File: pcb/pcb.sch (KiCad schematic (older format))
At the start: 20 parts, among them J1 BAT+, J2 BAT-, J3 Molex, SW1 Reset, SW2 Flash, U1 CP2102-BREAKOUT, U2 ESP-12F, U3 TP4056, U4 GY-521, U5 VREG

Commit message: Patent-unencumbered PCB concept
Tilting is off the table, so let's explore a different idea: weighing
a sinker immersed in the wort. See the github pages plog for more.
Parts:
- removed U4: GY-521, GY521:GY521, symbol GY-521
- added D1, D2: D, Diodes_SMD:D_0805, symbol D
- added J10: GRN, Extra_Pads:SolderWirePad_single_SMD_5x3mm, symbol Conn_01x01
- added J11: RED, Extra_Pads:SolderWirePad_single_SMD_5x3mm, symbol Conn_01x01
- added J12: Load Cell, Connectors_Molex:Molex_PicoBlade_53048-0410_04x1.25mm_Angled, symbol Conn_01x04
- added J4: TMP37, Connectors_Molex:Molex_PicoBlade_53048-0310_03x1.25mm_Angled, symbol Conn_01x03
- added J5: TMP+, Extra_Pads:SolderWirePad_single_SMD_5x3mm, symbol Conn_01x01
- added J6: TMPO, Extra_Pads:SolderWirePad_single_SMD_5x3mm, symbol Conn_01x01
- added J7: TMP-, Extra_Pads:SolderWirePad_single_SMD_5x3mm, symbol Conn_01x01
- added J8: WHT, Extra_Pads:SolderWirePad_single_SMD_5x3mm, symbol Conn_01x01
- added J9: BLK, Extra_Pads:SolderWirePad_single_SMD_5x3mm, symbol Conn_01x01
- added Q1: BC847, TO_SOT_Packages_SMD:SOT-23, symbol BC847
- added R8: 10k, Resistors_SMD:R_0805, symbol R
- added U4: HX711_BREAKOUT, HX711-XNQ:HX711-XNQ, symbol HX711_BREAKOUT
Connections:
- net labels added: ADC, BLK, CLK, DAT, GRN, HX+, RED, SENS1, SENS2, TMP+, TMP-, TMPO, WHT
- net labels removed: GY+, SCL, SDA
- wire segments 61 -> 86
- no-connect marks 14 -> 10
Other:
- note added: "Battery Monitor"
- note added: "Battery Pads\n\n"
- note added: "Load Cell"
- note added: "TMP37 Molex/Pads"
- note removed: "Pad"
- moved on the sheet: C1, R1, R2, R3, R4, R5, R6, R7, SW1, SW2, U2

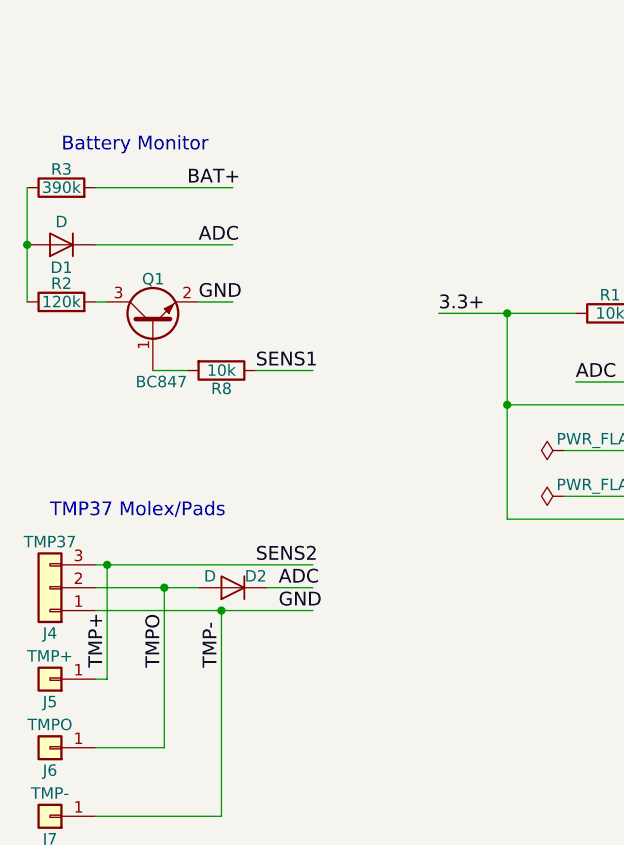
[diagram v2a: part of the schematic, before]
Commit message: Add a pad for a decoupling capacitor for temperature sensor, just in case
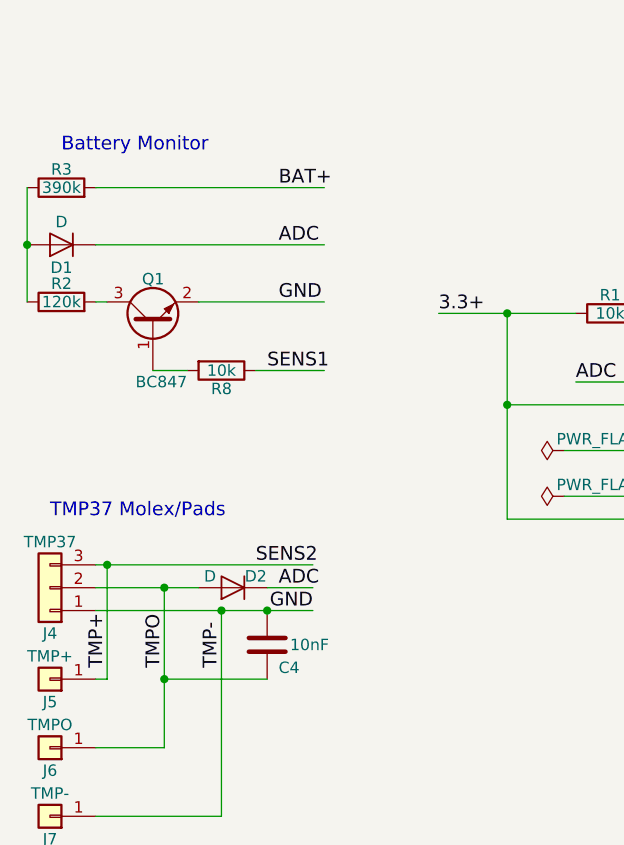
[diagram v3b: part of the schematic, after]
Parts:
- added C4: 10nF, Capacitors_SMD:C_0805, symbol C
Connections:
- wire segments 86 -> 87
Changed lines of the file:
@@
 Text Label 3800 2500 0    60   ~ 0
 USB-
-Text Label 1550 4250 0    60   ~ 0
+Text Label 1950 4250 0    60   ~ 0
 BAT+
 Text Label 6000 5200 0    60   ~ 0
@@
 	0    -1   -1   0
 $EndComp
-Text Label 1600 4750 0    60   ~ 0
+Text Label 1950 4750 0    60   ~ 0
 GND
 $Comp
@@
 	-1   0    0    1
 $EndComp
-Text Label 1600 4500 0    60   ~ 0
+Text Label 1950 4500 0    60   ~ 0
 ADC
 Text Label 3600 5500 0    60   ~ 0
@@
 	0    -1   -1   0
 $EndComp
-Text Label 1850 5050 0    60   ~ 0
+Text Label 1900 5050 0    60   ~ 0
 SENS1
 Text Notes 1000 4100 0    60   ~ 0
@@
 Text Label 1850 5900 0    60   ~ 0
 SENS2
-Text Label 1950 6100 0    60   ~ 0
+Text Label 2100 6100 2    60   ~ 0
 GND
 $Comp
@@
 	3950 5100 3250 5100
 Wire Wire Line
-	1150 4500 1750 4500
+	1150 4500 2150 4500
 Wire Wire Line
 	3600 5500 3950 5500
@@
 	3200 5600 3950 5600
 Wire Wire Line
-	1150 4250 1750 4250
+	1150 4250 2150 4250
 Wire Wire Line
 	850  4250 850  4750
@@
 	1150 4750 1200 4750
 Wire Wire Line
-	1600 4750 1750 4750
+	1600 4750 2150 4750
 Wire Wire Line
 	1150 5900 2100 5900
@@
 	1400 5050 1550 5050
 Wire Wire Line
-	1850 5050 2100 5050
+	1850 5050 2150 5050
+$Comp
+L C C4
+U 1 1 5B2A9325
+P 1900 6250
+F 0 "C4" H 1950 6150 50  0000 L CNN
+F 1 "10nF" H 2000 6250 50  0000 L CNN
+F 2 "Capacitors_SMD:C_0805" H 1938 6100 50  0001 C CNN
+F 3 "" H 1900 6250 50  0001 C CNN
+	1    1900 6250
+	1    0    0    -1
+$EndComp
+Connection ~ 1900 6100
+Wire Wire Line
+	1450 6400 1900 6400
+Connection ~ 1450 6400
 $EndSCHEMATC

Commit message: Measure some pictures of chips to update local parts libraries
Hopefully it's good enough. Otherwise we'll fix it in rev2.
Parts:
- U4: footprint HX711-XNQ:HX711-XNQ -> HX711-XNQ:HX711-MINI
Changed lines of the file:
@@
 F 0 "U4" H 9150 5250 60  0000 C CNN
 F 1 "HX711_BREAKOUT" H 9150 5900 60  0000 C CNN
-F 2 "HX711-XNQ:HX711-XNQ" H 8650 5850 60  0001 C CNN
+F 2 "HX711-XNQ:HX711-MINI" H 8650 5850 60  0001 C CNN
 F 3 "" H 8650 5850 60  0001 C CNN
 	1    8650 5850

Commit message: Fix some design errors, including a missing connection from 16->RST
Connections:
- wire segments 87 -> 89
- no-connect marks 10 -> 9
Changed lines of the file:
@@
 	0    1    1    0
 $EndComp
-NoConn ~ 3950 5300
 $Comp
 L C C3
@@
 	6300 5600 6450 5600
 Wire Wire Line
-	3900 5000 3950 5000
+	3650 5000 3950 5000
 Wire Wire Line
 	5400 2250 5400 1950
@@
 	1450 6400 1900 6400
 Connection ~ 1450 6400
+Wire Wire Line
+	3950 5300 3650 5300
+Wire Wire Line
+	3650 5300 3650 5000
+Connection ~ 3900 5000
 $EndSCHEMATC

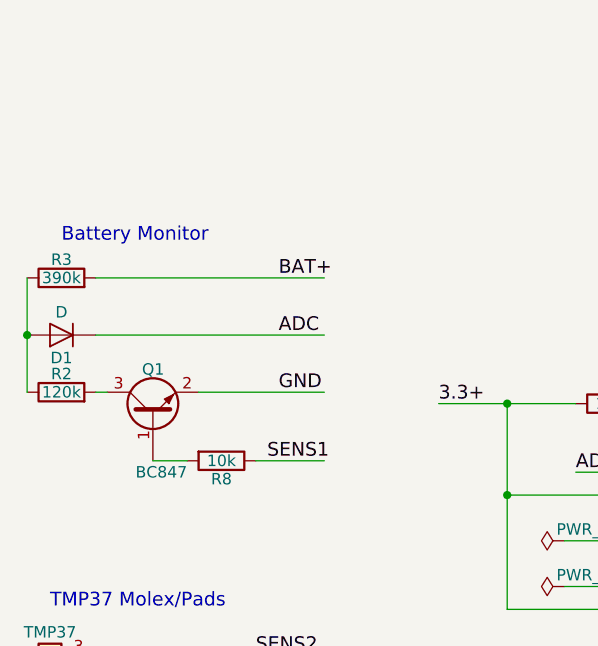
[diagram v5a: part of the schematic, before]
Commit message: Switch to p-channel MOSFET for battery monitor switch
Because we want as close to zero voltage through the circuit to the
ADC as possible when the battery monitor is off and the temperature
sensor is on, we need to switch on the high side, between BAT+ and
ADC.

The BSS84 seems like a reasonable choice; its maximum gate threshold
voltage is well below the difference between ground and a discharged
li-ion at 2.7V. I don't really care about pulling it up to 3.3 so
that it keeps the battery circuit off; it's the difference between
a hundred nanoamps and six or eight microamps.
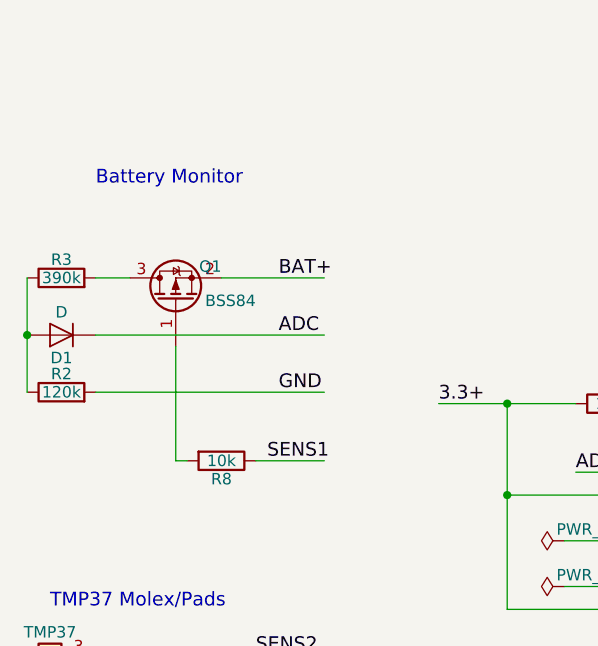
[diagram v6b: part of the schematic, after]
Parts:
- removed Q1: BC847, TO_SOT_Packages_SMD:SOT-23, symbol BC847
- added Q1: BSS84, TO_SOT_Packages_SMD:SOT-23, symbol BSS84
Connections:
- wire segments 89 -> 90
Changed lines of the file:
@@
 Text Label 3600 5400 0    60   ~ 0
 SENS2
-$Comp
-L BC847 Q1
-U 1 1 5B296BA7
-P 1400 4850
-F 0 "Q1" V 1600 4800 50  0000 L CNN
-F 1 "BC847" V 1150 4700 50  0000 L CNN
-F 2 "TO_SOT_Packages_SMD:SOT-23" H 1600 4775 50  0001 L CIN
-F 3 "" H 1400 4850 50  0001 L CNN
-	1    1400 4850
-	0    -1   -1   0
-$EndComp
 Text Label 1900 5050 0    60   ~ 0
 SENS1
-Text Notes 1000 4100 0    60   ~ 0
+Text Notes 1150 3850 0    60   ~ 0
 Battery Monitor
 $Comp
@@
 	3200 5600 3950 5600
 Wire Wire Line
-	1150 4250 2150 4250
-Wire Wire Line
 	850  4250 850  4750
 Connection ~ 850  4500
 Wire Wire Line
-	1150 4750 1200 4750
-Wire Wire Line
-	1600 4750 2150 4750
+	1150 4750 2150 4750
 Wire Wire Line
 	1150 5900 2100 5900
@@
 $EndComp
 Wire Wire Line
-	1400 5050 1550 5050
-Wire Wire Line
 	1850 5050 2150 5050
 $Comp
@@
 	3650 5300 3650 5000
 Connection ~ 3900 5000
+$Comp
+L BSS84 Q1
+U 1 1 5B2BFF6A
+P 1500 4350
+F 0 "Q1" V 1650 4150 50  0000 L CNN
+F 1 "BSS84" V 1500 4000 50  0000 L CNN
+F 2 "TO_SOT_Packages_SMD:SOT-23" H 1700 4275 50  0001 L CIN
+F 3 "" H 1500 4350 50  0001 L CNN
+	1    1500 4350
+	0    -1   -1   0
+$EndComp
+Wire Wire Line
+	1150 4250 1300 4250
+Wire Wire Line
+	1700 4250 2150 4250
+Wire Wire Line
+	1500 4550 1500 5050
+Wire Wire Line
+	1500 5050 1550 5050
 $EndSCHEMATC

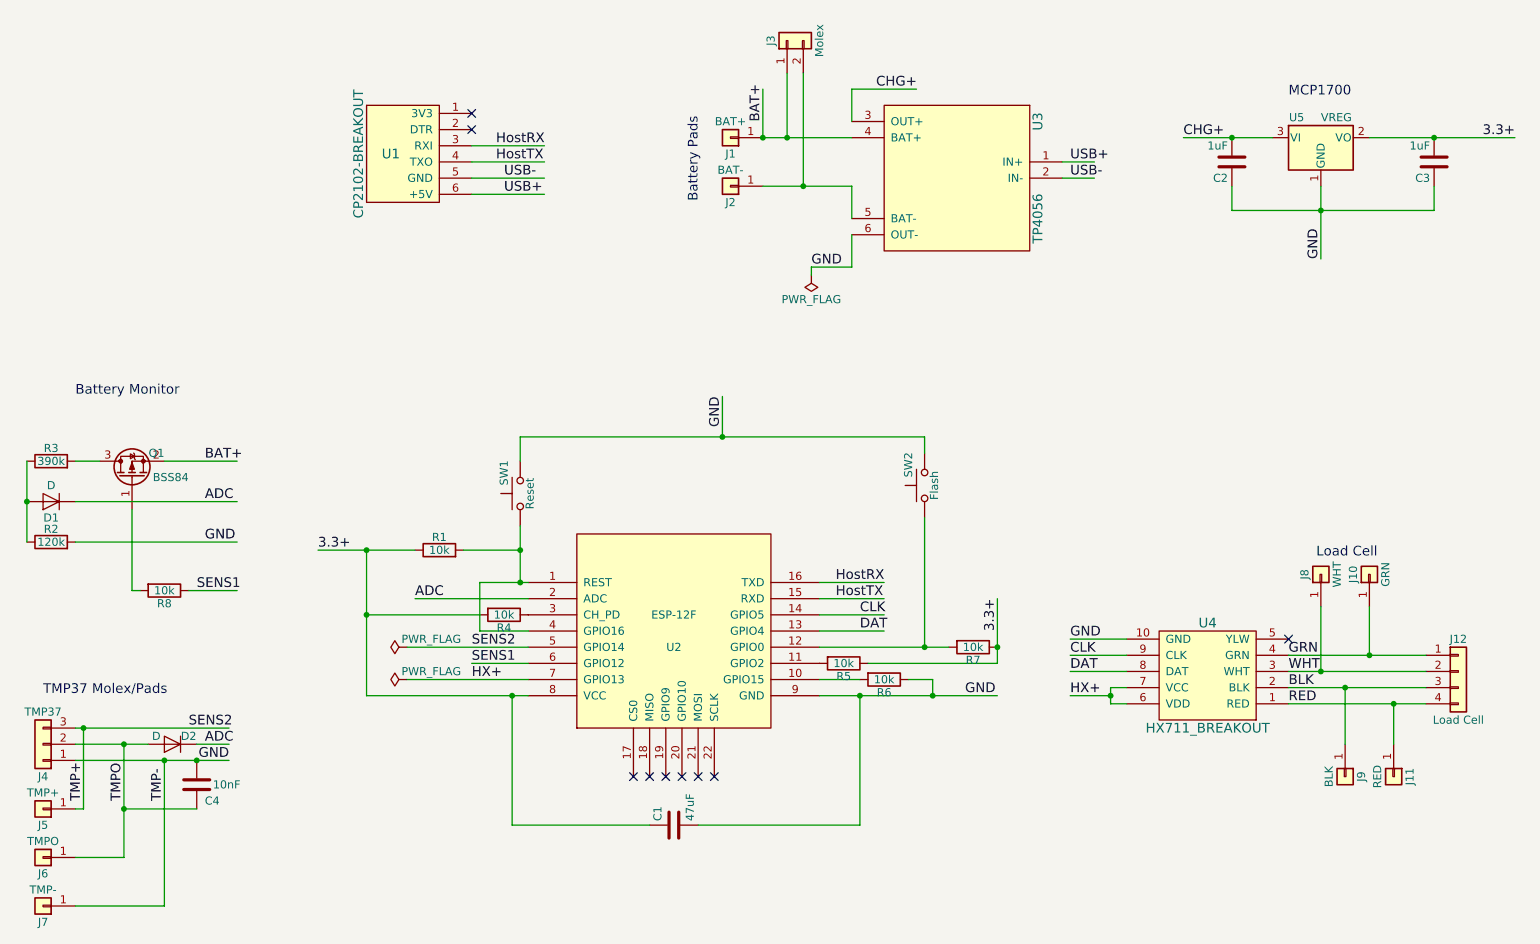
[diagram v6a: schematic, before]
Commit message: DS18B20, 4x3 switch footprint, routing tweaks
Use a DS18B20 temperature sensor instead of a TMP36. We have enough
GPIOs—we can drive it from the former SENS2 net (power for the prior
sensor) and use the former SENS1 net (battery monitor transistor) for
the data line. This simplifies the ADC circuitry significantly, and
lets us ditch a bunch of parts.

Add 4mmx3mm switch footprint, adjust routing as needed.
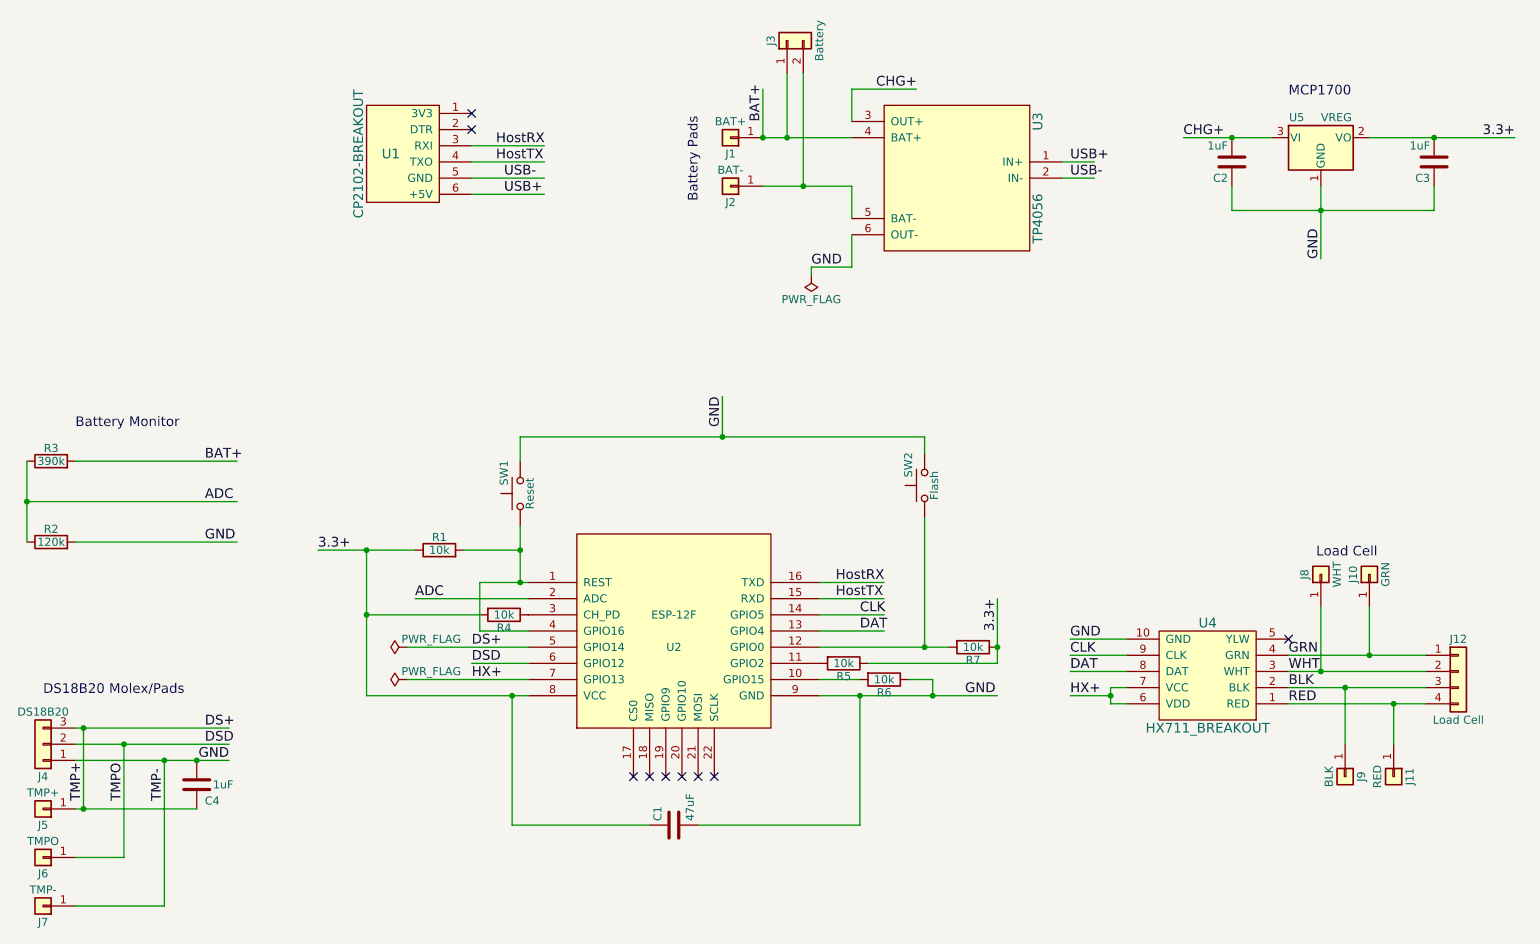
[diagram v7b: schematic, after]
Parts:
- removed D1, D2: D, Diodes_SMD:D_0805, symbol D
- removed Q1: BSS84, TO_SOT_Packages_SMD:SOT-23, symbol BSS84
- removed R8: 10k, Resistors_SMD:R_0805, symbol R
- C4: value 10nF -> 1uF
- J3: value Molex -> Battery
- J4: value TMP37 -> DS18B20
- SW1, SW2: footprint Buttons_Switches_SMD:SW_SPST_B3U-1000P -> 4x3_SWITCH:4x3_Switch
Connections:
- net labels added: DS+, DSD
- net labels removed: SENS1, SENS2
- wire segments 90 -> 84
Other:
- note added: "DS18B20 Molex/Pads"
- note removed: "TMP37 Molex/Pads"
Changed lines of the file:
@@
 F 0 "SW2" H 6450 4500 50  0000 L CNN
 F 1 "Flash" H 6400 4340 50  0000 C CNN
-F 2 "Buttons_Switches_SMD:SW_SPST_B3U-1000P" H 6400 4600 50  0001 C CNN
+F 2 "4x3_SWITCH:4x3_Switch" H 6400 4600 50  0001 C CNN
 F 3 "" H 6400 4600 50  0001 C CNN
 	1    6400 4400
@@
 F 0 "SW1" H 3950 4550 50  0000 L CNN
 F 1 "Reset" H 3900 4390 50  0000 C CNN
-F 2 "Buttons_Switches_SMD:SW_SPST_B3U-1000P" H 3900 4650 50  0001 C CNN
+F 2 "4x3_SWITCH:4x3_Switch" H 3900 4650 50  0001 C CNN
 F 3 "" H 3900 4650 50  0001 C CNN
 	1    3900 4450
@@
 P 5550 1650
 F 0 "J3" H 5550 1750 50  0000 C CNN
-F 1 "Molex" H 5550 1450 50  0000 C CNN
+F 1 "Battery" H 5550 1450 50  0000 C CNN
 F 2 "Connectors_Molex:Molex_PicoBlade_53048-0210_02x1.25mm_Angled" H 5550 1650 50  0001 C CNN
 F 3 "" H 5550 1650 50  0001 C CNN
@@
 Text Label 3250 5100 0    60   ~ 0
 ADC
-$Comp
-L D D1
-U 1 1 5B294D94
-P 1000 4500
-F 0 "D1" H 1000 4600 50  0000 C CNN
-F 1 "D" H 1000 4400 50  0000 C CNN
-F 2 "Diodes_SMD:D_0805" H 1000 4500 50  0001 C CNN
-F 3 "" H 1000 4500 50  0001 C CNN
-	1    1000 4500
-	-1   0    0    1
-$EndComp
 Text Label 1950 4500 0    60   ~ 0
 ADC
 Text Label 3600 5500 0    60   ~ 0
-SENS1
+DSD
 Text Label 3600 5400 0    60   ~ 0
-SENS2
-Text Label 1900 5050 0    60   ~ 0
-SENS1
-Text Notes 1150 3850 0    60   ~ 0
+DS+
+Text Notes 1150 4050 0    60   ~ 0
 Battery Monitor
-$Comp
-L D D2
-U 1 1 5B298970
-P 1750 6000
-F 0 "D2" H 1650 5950 50  0000 C CNN
-F 1 "D" H 1850 5950 50  0000 C CNN
-F 2 "Diodes_SMD:D_0805" H 1750 6000 50  0001 C CNN
-F 3 "" H 1750 6000 50  0001 C CNN
-	1    1750 6000
-	-1   0    0    1
-$EndComp
 Text Label 1950 6000 0    60   ~ 0
-ADC
-Text Label 1850 5900 0    60   ~ 0
-SENS2
+DSD
+Text Label 1950 5900 0    60   ~ 0
+DS+
 Text Label 2100 6100 2    60   ~ 0
 GND
@@
 P 950 6000
 F 0 "J4" H 950 6200 50  0000 C CNN
-F 1 "TMP37" H 950 5800 50  0000 C CNN
+F 1 "DS18B20" H 950 5800 50  0000 C CNN
 F 2 "Connectors_Molex:Molex_PicoBlade_53048-0310_03x1.25mm_Angled" H 950 6000 50  0001 C CNN
 F 3 "" H 950 6000 50  0001 C CNN
@@
 $EndComp
 Text Notes 950  5700 0    60   ~ 0
-TMP37 Molex/Pads
+DS18B20 Molex/Pads
 $Comp
 L Conn_01x01 J5
@@
 	3950 5100 3250 5100
 Wire Wire Line
-	1150 4500 2150 4500
+	850  4500 2150 4500
 Wire Wire Line
 	3600 5500 3950 5500
@@
 	1150 5900 2100 5900
 Wire Wire Line
-	1900 6000 2100 6000
+	1150 6000 2100 6000
 Wire Wire Line
 	1150 6100 2100 6100
-Wire Wire Line
-	1150 6000 1600 6000
 Wire Wire Line
 	1200 5900 1200 6400
@@
 Connection ~ 1700 6100
 Wire Wire Line
-	1200 6400 1150 6400
+	1150 6400 1900 6400
 Wire Wire Line
 	1450 6700 1150 6700
@@
 $EndComp
 $Comp
-L R R8
-U 1 1 5B2971BE
-P 1700 5050
-F 0 "R8" V 1780 5050 50  0000 C CNN
-F 1 "10k" V 1700 5050 50  0000 C CNN
-F 2 "Resistors_SMD:R_0805" V 1630 5050 50  0001 C CNN
-F 3 "" H 1700 5050 50  0001 C CNN
-	1    1700 5050
-	0    1    1    0
-$EndComp
-Wire Wire Line
-	1850 5050 2150 5050
-$Comp
 L C C4
 U 1 1 5B2A9325
 P 1900 6250
 F 0 "C4" H 1950 6150 50  0000 L CNN
-F 1 "10nF" H 2000 6250 50  0000 L CNN
+F 1 "1uF" H 2000 6250 50  0000 L CNN
 F 2 "Capacitors_SMD:C_0805" H 1938 6100 50  0001 C CNN
 F 3 "" H 1900 6250 50  0001 C CNN
@@
 Connection ~ 1900 6100
 Wire Wire Line
-	1450 6400 1900 6400
-Connection ~ 1450 6400
-Wire Wire Line
 	3950 5300 3650 5300
 Wire Wire Line
 	3650 5300 3650 5000
 Connection ~ 3900 5000
-$Comp
-L BSS84 Q1
-U 1 1 5B2BFF6A
-P 1500 4350
-F 0 "Q1" V 1650 4150 50  0000 L CNN
-F 1 "BSS84" V 1500 4000 50  0000 L CNN
-F 2 "TO_SOT_Packages_SMD:SOT-23" H 1700 4275 50  0001 L CIN
-F 3 "" H 1500 4350 50  0001 L CNN
-	1    1500 4350
-	0    -1   -1   0
-$EndComp
-Wire Wire Line
-	1150 4250 1300 4250
-Wire Wire Line
-	1700 4250 2150 4250
-Wire Wire Line
-	1500 4550 1500 5050
-Wire Wire Line
-	1500 5050 1550 5050
+Wire Wire Line
+	1150 4250 2150 4250
+Connection ~ 1200 6400
 $EndSCHEMATC
